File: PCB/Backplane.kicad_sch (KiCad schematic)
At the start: 120 parts, among them J1 L_XLR_In, J10 R_Pre_Out, J11 TRS_Out, J12 RCA_Pre_Out, J13 DD21.0121.1111, J14 ICSP, J2 R_XLR_In, J3 RCA_In, J8 XLR_Out, J9 L_Pre_Out, K1 G6K-2, K2 G6K-2, K3 G6K-2, K4 G6K-2, K5 G6K-2, K6 G6K-2, K7 G6K-2, K8 G5LE-1, SW1 Reset, SW2 Input mode, SW3 Standby, SW4 Output mode, U1 LM339, U10 ATtiny2313A-P, U11 ULN2803A, U12 MC7812ACTG, U13 MC7912ACTG, U14 Attenuator, U2 LM339, U3 Attenuator, U4 Amp_Module, U5 Amp_Module, U6 Amp_Module, U7 Amp_Module, U8 74LS02, U9 LM393, Y1 16M

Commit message: Added images, fixed gerbers, fixed attenuator silk
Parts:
- R14, R15, R16, R17, R27, R28, R31, R32: value 22 -> 47
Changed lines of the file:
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@@
     (in_bom yes) (on_board yes) (fields_autoplaced)
     (property "Reference" "R32" (id 0) (at 203.2 125.73 90))
-    (property "Value" "22" (id 1) (at 203.2 128.27 90))
+    (property "Value" "47" (id 1) (at 203.2 128.27 90))
     (property "Footprint" "Resistor_SMD:R_1206_3216Metric" (id 2) (at 203.2 121.92 0)
       (effects (font (size 1.27 1.27)) hide)
@@
     (in_bom yes) (on_board yes) (fields_autoplaced)
     (property "Reference" "R17" (id 0) (at 203.2 113.03 90))
-    (property "Value" "22" (id 1) (at 203.2 115.57 90))
+    (property "Value" "47" (id 1) (at 203.2 115.57 90))
     (property "Footprint" "Resistor_SMD:R_1206_3216Metric" (id 2) (at 203.2 119.38 0)
       (effects (font (size 1.27 1.27)) hide)
@@
     (in_bom yes) (on_board yes) (fields_autoplaced)
     (property "Reference" "R16" (id 0) (at 203.2 87.63 90))
-    (property "Value" "22" (id 1) (at 203.2 90.17 90))
+    (property "Value" "47" (id 1) (at 203.2 90.17 90))
     (property "Footprint" "Resistor_SMD:R_1206_3216Metric" (id 2) (at 203.2 93.98 0)
       (effects (font (size 1.27 1.27)) hide)
@@
     (in_bom yes) (on_board yes) (fields_autoplaced)
     (property "Reference" "R14" (id 0) (at 203.2 31.75 90))
-    (property "Value" "22" (id 1) (at 203.2 34.29 90))
+    (property "Value" "47" (id 1) (at 203.2 34.29 90))
     (property "Footprint" "Resistor_SMD:R_1206_3216Metric" (id 2) (at 203.2 38.1 0)
       (effects (font (size 1.27 1.27)) hide)
@@
     (in_bom yes) (on_board yes) (fields_autoplaced)
     (property "Reference" "R31" (id 0) (at 203.2 100.33 90))
-    (property "Value" "22" (id 1) (at 203.2 102.87 90))
+    (property "Value" "47" (id 1) (at 203.2 102.87 90))
     (property "Footprint" "Resistor_SMD:R_1206_3216Metric" (id 2) (at 203.2 96.52 0)
       (effects (font (size 1.27 1.27)) hide)
@@
     (in_bom yes) (on_board yes) (fields_autoplaced)
     (property "Reference" "R15" (id 0) (at 203.2 57.15 90))
-    (property "Value" "22" (id 1) (at 203.2 59.69 90))
+    (property "Value" "47" (id 1) (at 203.2 59.69 90))
     (property "Footprint" "Resistor_SMD:R_1206_3216Metric" (id 2) (at 203.2 63.5 0)
       (effects (font (size 1.27 1.27)) hide)
@@
     (in_bom yes) (on_board yes) (fields_autoplaced)
     (property "Reference" "R28" (id 0) (at 203.2 69.85 90))
-    (property "Value" "22" (id 1) (at 203.2 72.39 90))
+    (property "Value" "47" (id 1) (at 203.2 72.39 90))
     (property "Footprint" "Resistor_SMD:R_1206_3216Metric" (id 2) (at 203.2 66.04 0)
       (effects (font (size 1.27 1.27)) hide)
@@
     (in_bom yes) (on_board yes) (fields_autoplaced)
     (property "Reference" "R27" (id 0) (at 203.2 44.45 90))
-    (property "Value" "22" (id 1) (at 203.2 46.99 90))
+    (property "Value" "47" (id 1) (at 203.2 46.99 90))
     (property "Footprint" "Resistor_SMD:R_1206_3216Metric" (id 2) (at 203.2 40.64 0)
       (effects (font (size 1.27 1.27)) hide)
@@
     )
     (path "/75ffe329-355e-41e4-b029-c94b31f6c314"
-      (reference "R14") (unit 1) (value "22") (footprint "Resistor_SMD:R_1206_3216Metric")
+      (reference "R14") (unit 1) (value "47") (footprint "Resistor_SMD:R_1206_3216Metric")
     )
     (path "/8a6b2355-2083-4b13-86a0-746c284b9ca0"
-      (reference "R15") (unit 1) (value "22") (footprint "Resistor_SMD:R_1206_3216Metric")
+      (reference "R15") (unit 1) (value "47") (footprint "Resistor_SMD:R_1206_3216Metric")
     )
     (path "/5f7ba5b7-9636-426f-8fa5-9f3a973963a8"
-      (reference "R16") (unit 1) (value "22") (footprint "Resistor_SMD:R_1206_3216Metric")
+      (reference "R16") (unit 1) (value "47") (footprint "Resistor_SMD:R_1206_3216Metric")
     )
     (path "/463cce41-ed03-46ba-9467-30226cb73ad3"
-      (reference "R17") (unit 1) (value "22") (footprint "Resistor_SMD:R_1206_3216Metric")
+      (reference "R17") (unit 1) (value "47") (footprint "Resistor_SMD:R_1206_3216Metric")
     )
     (path "/1e6e1d6c-40f7-4f3e-ae2e-04e4523ae8e1"
@@
     )
     (path "/cb0464e8-7841-40d5-a834-9171074a68d5"
-      (reference "R27") (unit 1) (value "22") (footprint "Resistor_SMD:R_1206_3216Metric")
+      (reference "R27") (unit 1) (value "47") (footprint "Resistor_SMD:R_1206_3216Metric")
     )
     (path "/b3bbe501-ee69-4538-bdc3-dca183c0d807"
-      (reference "R28") (unit 1) (value "22") (footprint "Resistor_SMD:R_1206_3216Metric")
+      (reference "R28") (unit 1) (value "47") (footprint "Resistor_SMD:R_1206_3216Metric")
     )
     (path "/c91587fa-197f-4dac-86ff-b50f4b5e19e5"
@@
     )
     (path "/8210dcab-4335-45ed-b4f7-51701736a6e7"
-      (reference "R31") (unit 1) (value "22") (footprint "Resistor_SMD:R_1206_3216Metric")
+      (reference "R31") (unit 1) (value "47") (footprint "Resistor_SMD:R_1206_3216Metric")
     )
     (path "/0189e5b8-19df-462d-8281-14ee0ce4c080"
-      (reference "R32") (unit 1) (value "22") (footprint "Resistor_SMD:R_1206_3216Metric")
+      (reference "R32") (unit 1) (value "47") (footprint "Resistor_SMD:R_1206_3216Metric")
     )
     (path "/a9faad41-c4ed-45fa-a949-05c8ebc86393"

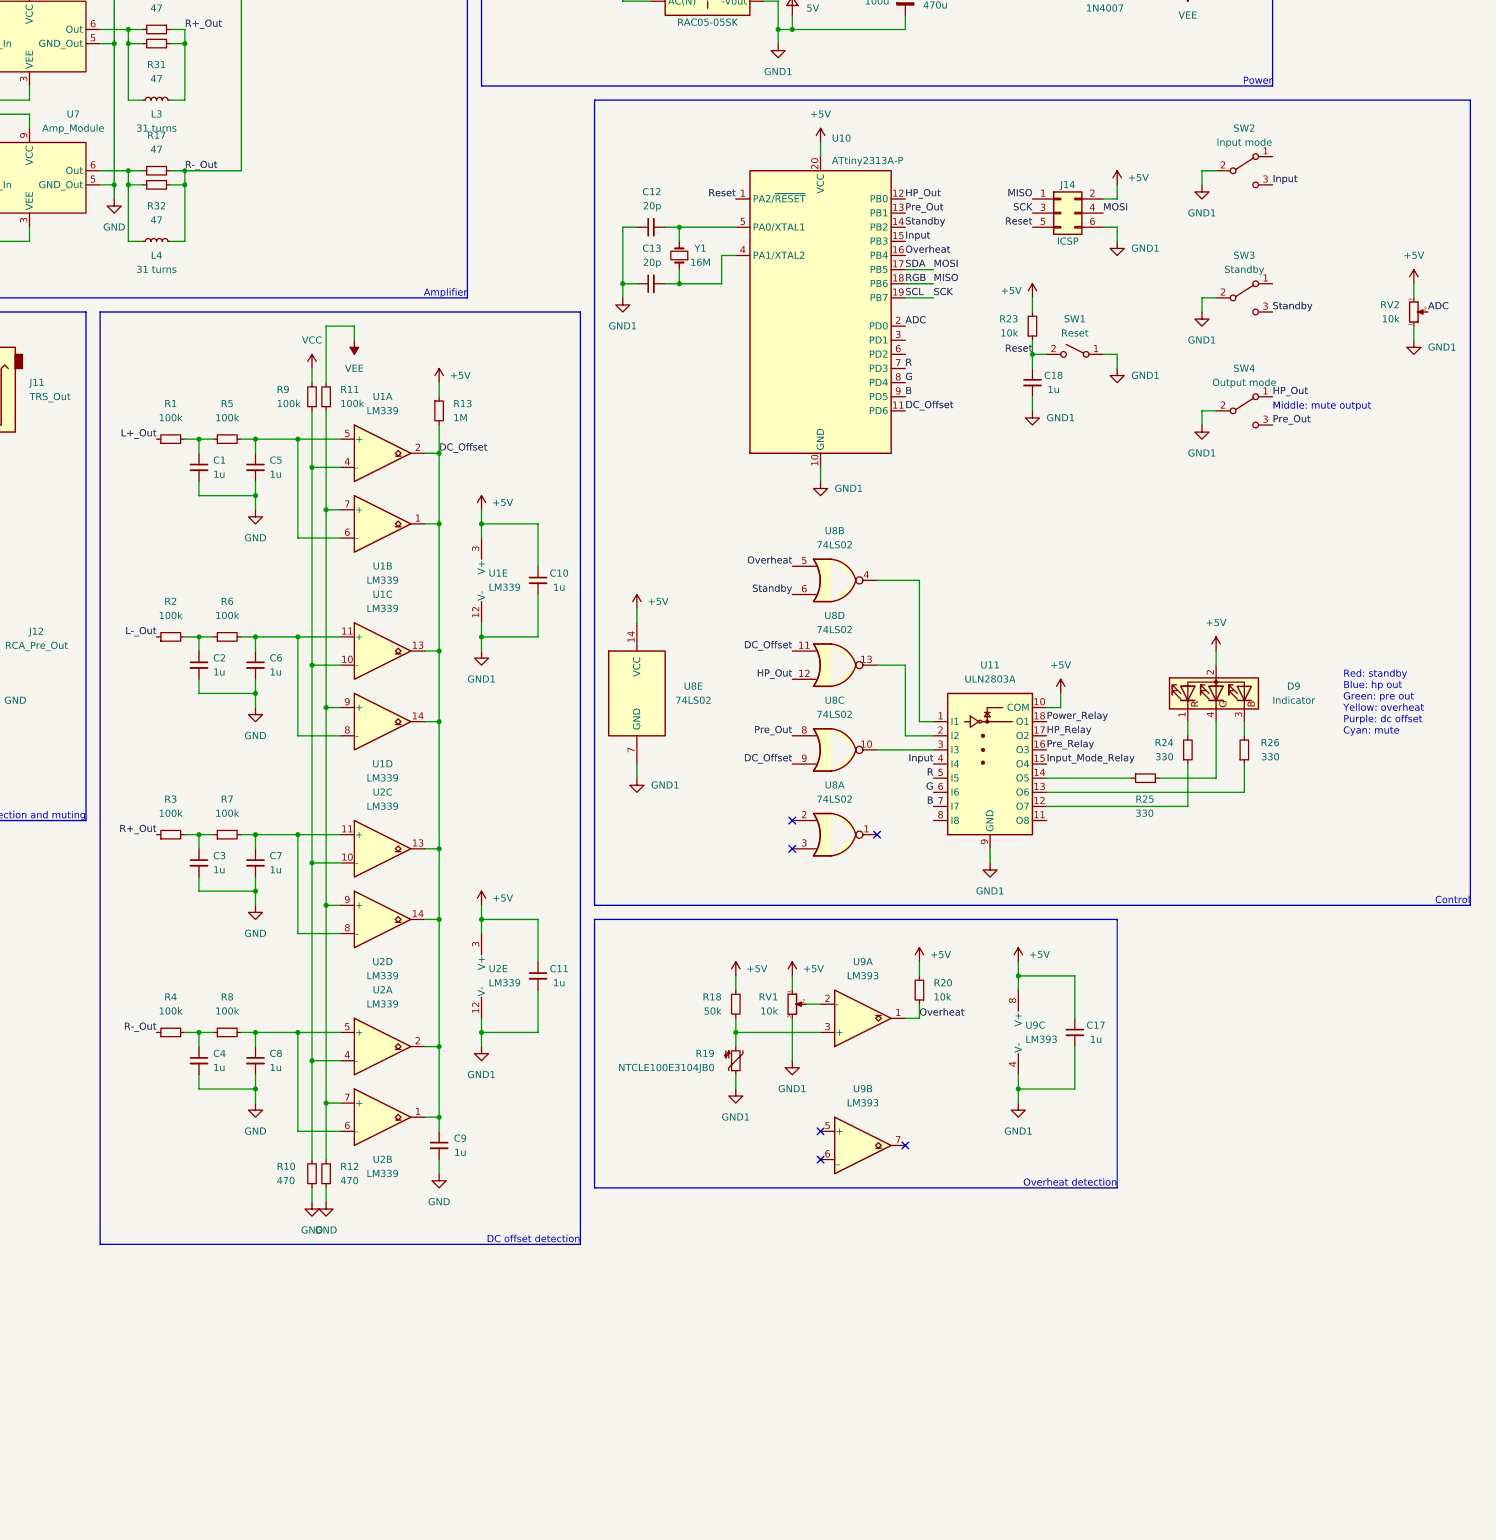
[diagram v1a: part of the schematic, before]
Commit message: Added 1u decoupling capacitors to ICs on backplane and attenuator boards
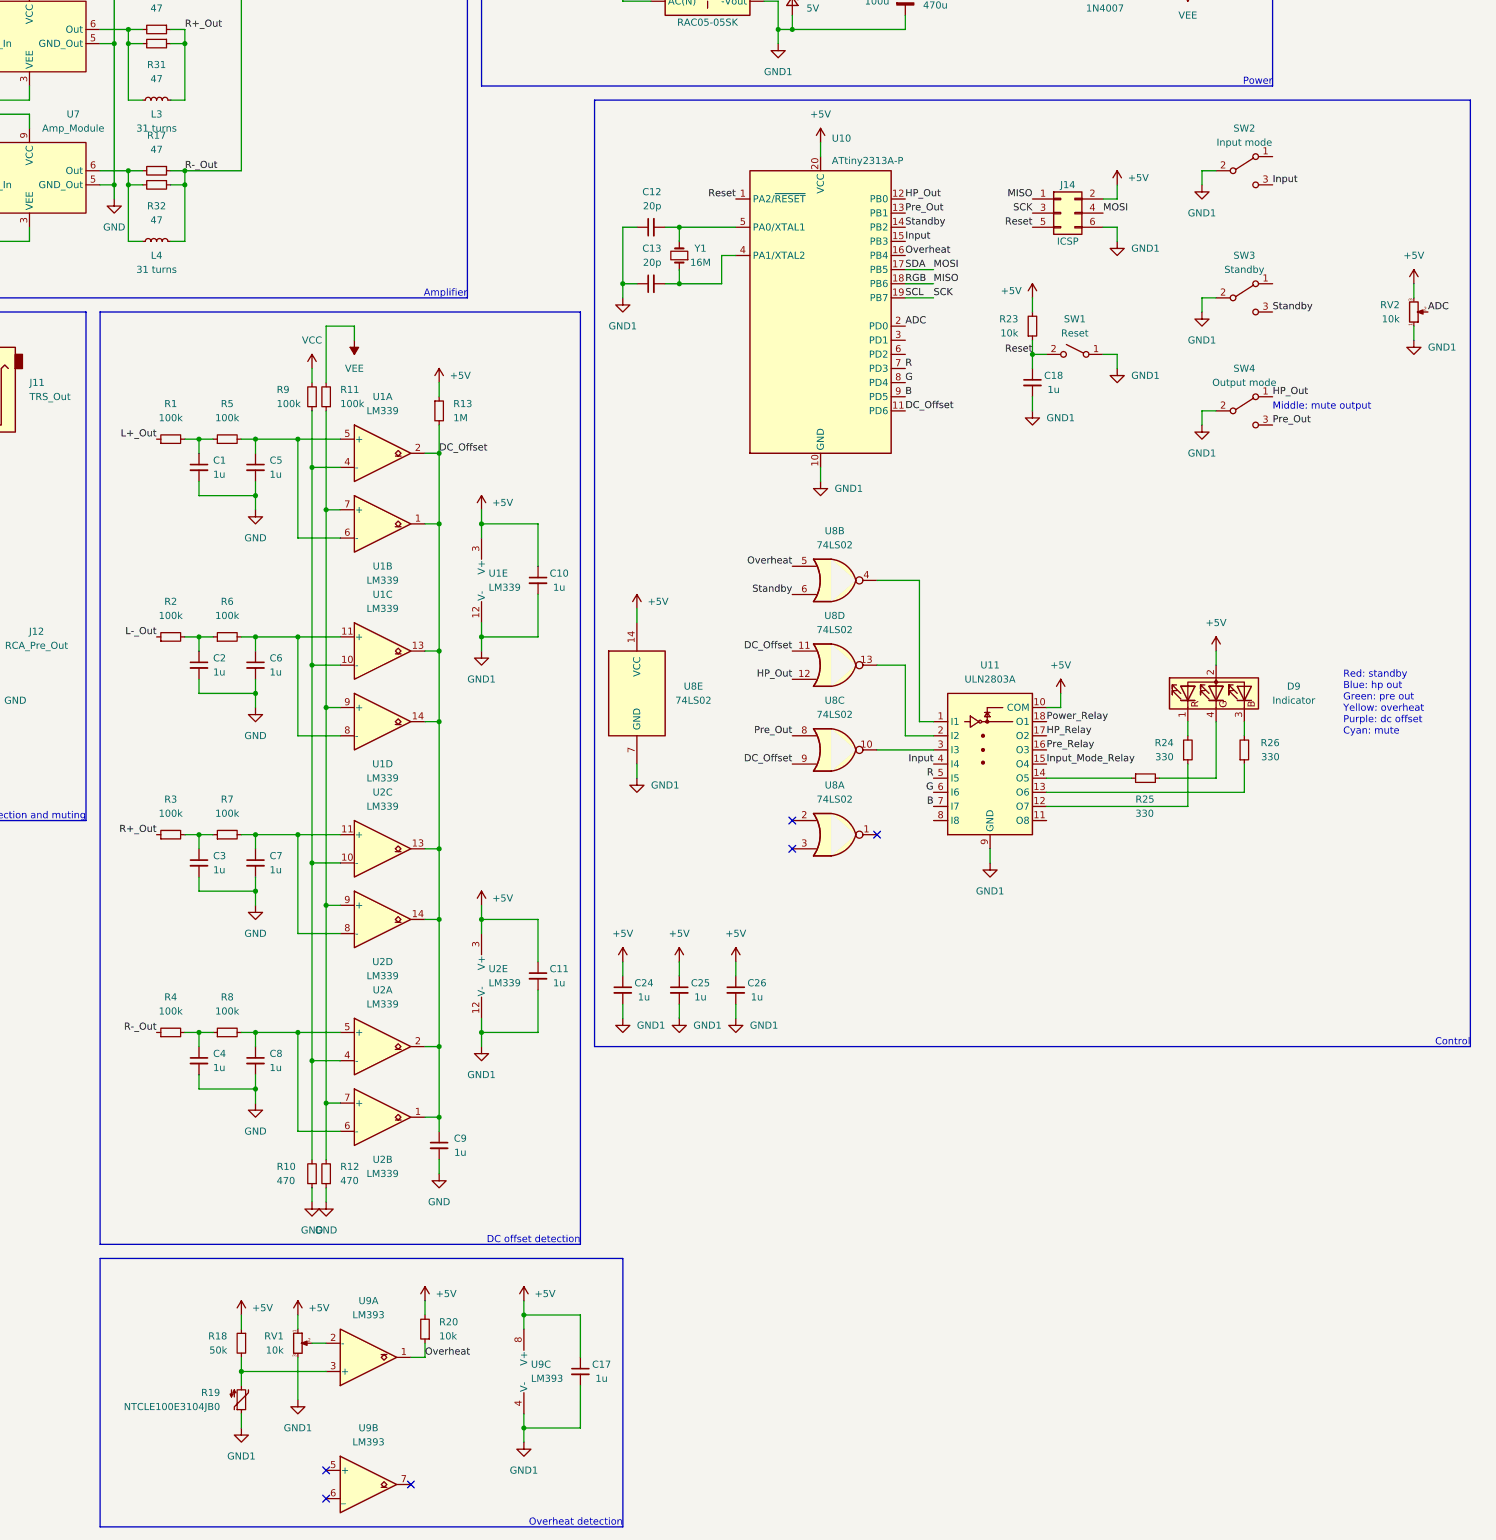
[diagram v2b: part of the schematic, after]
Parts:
- added C24, C25, C26: 1u, Capacitor_SMD:C_0603_1608Metric, symbol Device:C_Small
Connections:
- net +5V: now also C24.1, C25.1, C26.1
- net GND1: now also C24.2, C25.2, C26.2
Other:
- moved on the sheet: C17, R18, R19, R20, RV1, U9A, U9B, U9C
